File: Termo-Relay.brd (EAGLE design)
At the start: 53 x 61.6 mm, 50 parts, among them CN1 PBS-2-VERTICAL, CN2 PBS-2-VERTICAL, CN3 PBS-2-VERTICAL, CN5 PBS-4-VERTICAL, IC1 74HCT595D, IC2 74HCT595D, IC3 STM8S103FP, Q2 16M, T1 2N2222, T2 2N2222, T3 2N2222, T4 2N2222

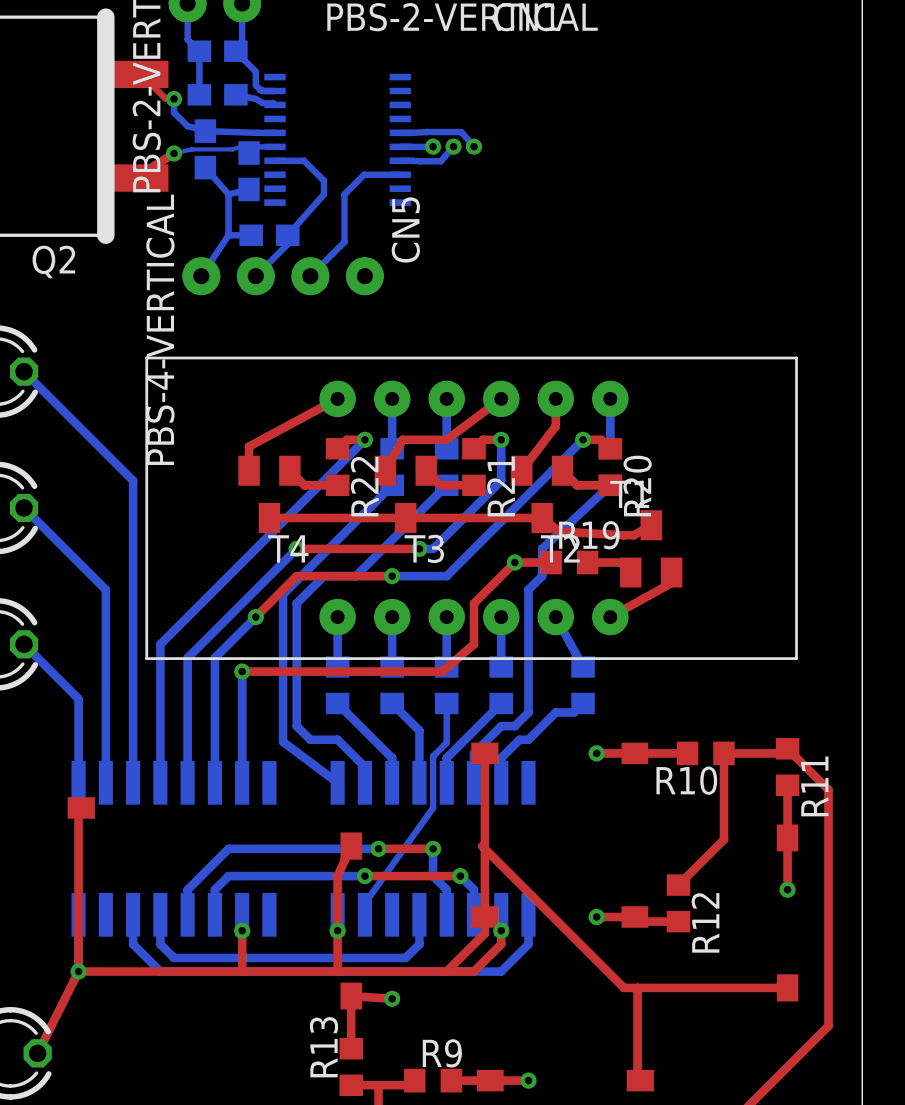
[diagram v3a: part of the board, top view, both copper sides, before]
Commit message: Roads for RCK, SCK and SER (between stm8 and hc595) were added
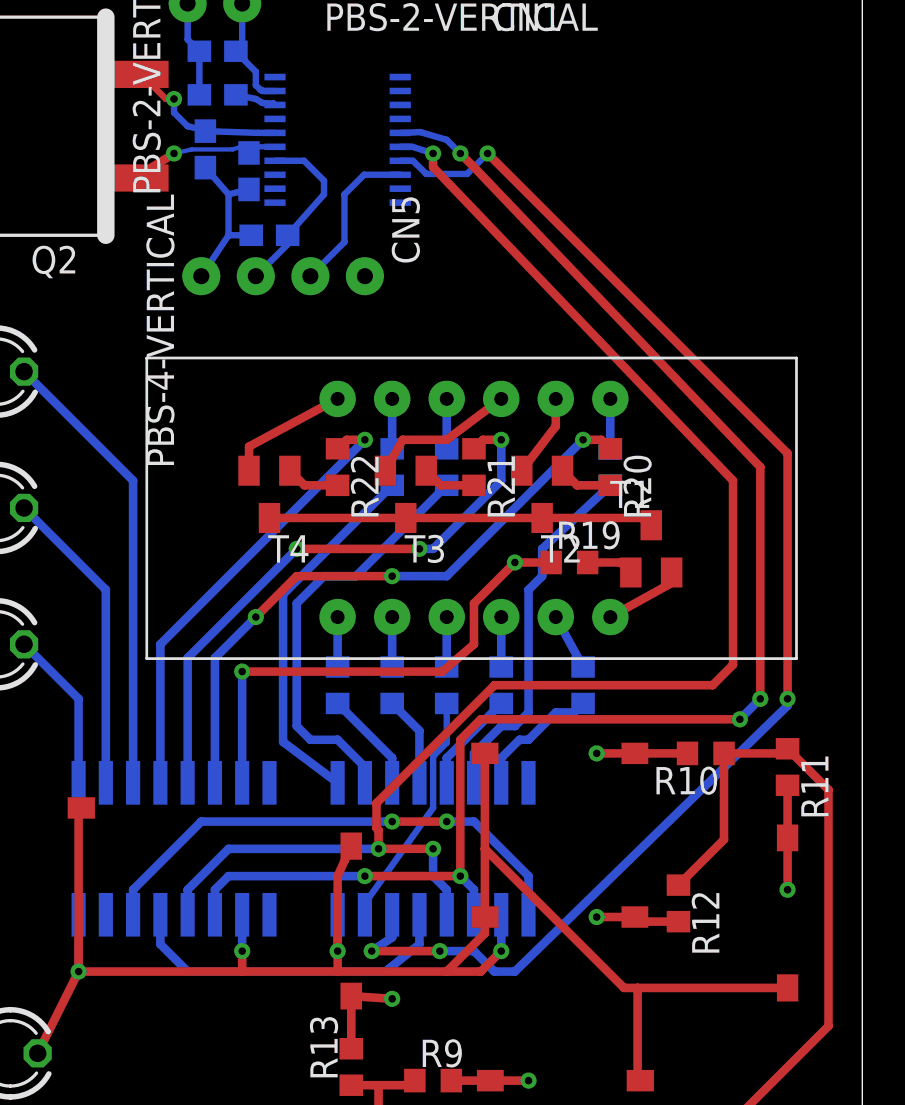
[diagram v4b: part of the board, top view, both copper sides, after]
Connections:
- net RCK: now also IC3.16; no longer IC3.15
- net SCK: now also IC3.15; no longer IC3.16
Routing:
- net SER: track 3.53 -> 63.2 mm, vias 1 -> 4
- net SCK: track 16.5 -> 70.2 mm, vias 3 -> 5
- net RCK: track 20.5 -> 69.2 mm
- net N$1: track 22.2 -> 23.8 mm, vias 0 -> 2
- net VCC: track 101.3 -> 102.1 mm

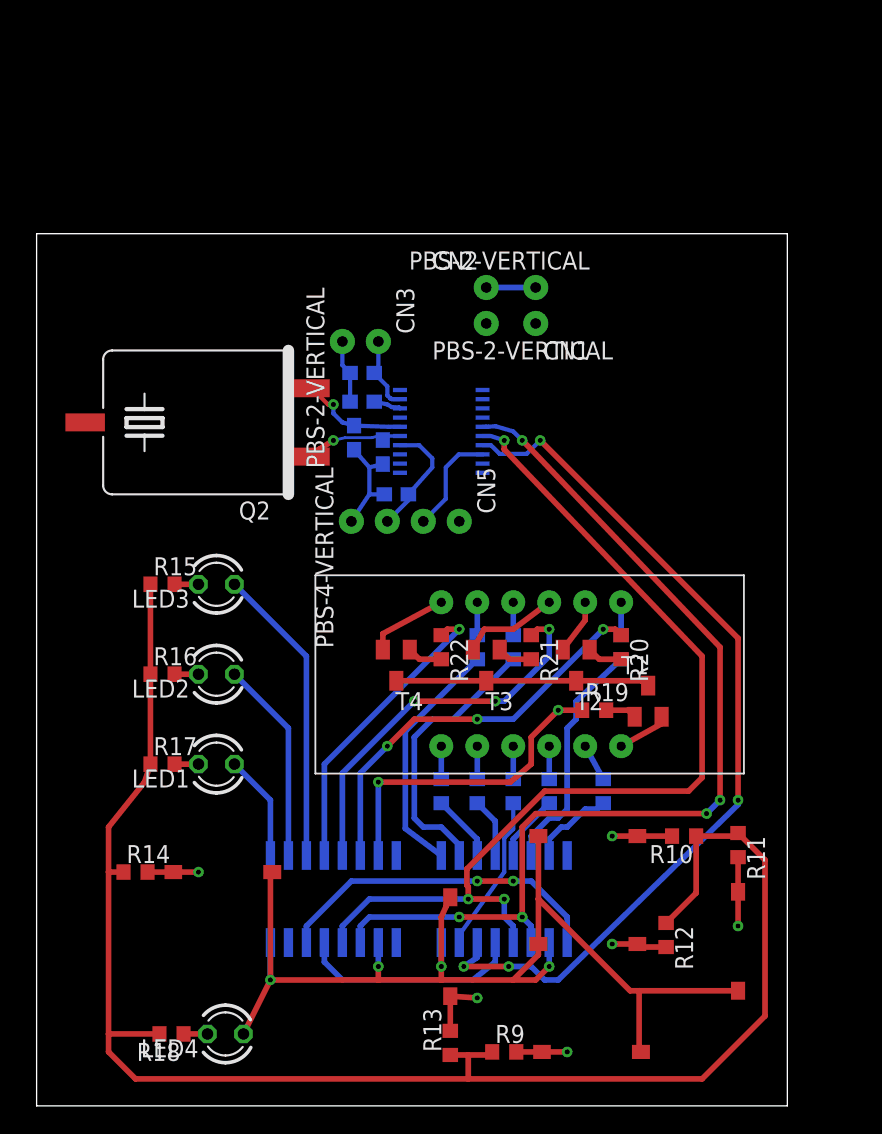
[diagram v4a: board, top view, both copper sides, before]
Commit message: size of the board was smalled
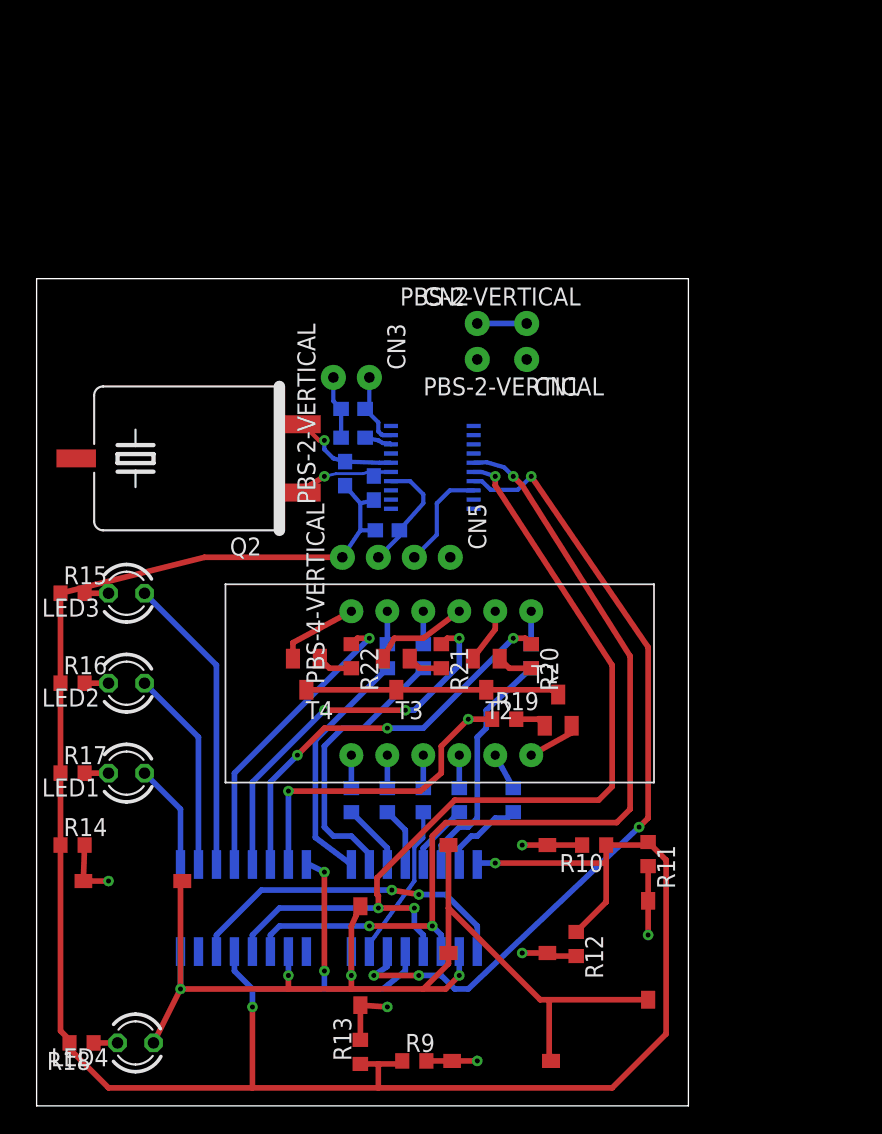
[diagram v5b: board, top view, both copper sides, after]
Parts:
- moved BTN4 6.38 mm to (22.9, 7.62)
- moved BTN5 6.38 mm to (43.2, 14.0)
- moved BTN6 6.38 mm to (29.8, 3.17)
- moved DISPLAY1 6.38 mm to (29.8, 29.8)
- moved IC1 6.38 mm to (26.7, 14.0)
- moved R1 6.38 mm to (27.3, 21.6)
- moved R10 6.38 mm to (39.4, 18.4)
- moved R11 6.38 mm to (43.2, 17.8)
- moved R12 6.38 mm to (38.1, 11.4)
- moved R13 6.38 mm to (22.9, 3.81)
- moved R2 6.38 mm to (33.7, 21.6)
- moved R20 6.38 mm to (34.9, 31.8)
- moved R3 6.38 mm to (34.9, 31.8)
- moved R4 6.38 mm to (29.8, 21.6)
- moved R7 6.38 mm to (27.3, 31.8)
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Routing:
- net GND: track 147.8 -> 184.2 mm, vias 0 -> 4
- net RCK: track 69.2 -> 64.1 mm
- net SCK: track 70.2 -> 65.1 mm, vias 5 -> 3
- net SER: track 63.2 -> 58.2 mm
- net BTN_INDIC: track 3.59 -> 4.32 mm
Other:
- board size 53 x 61.6 mm -> 46 x 58.4 mm

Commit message: Roads for buttons and power were added. One error (center button was not connected to STM) was corrected
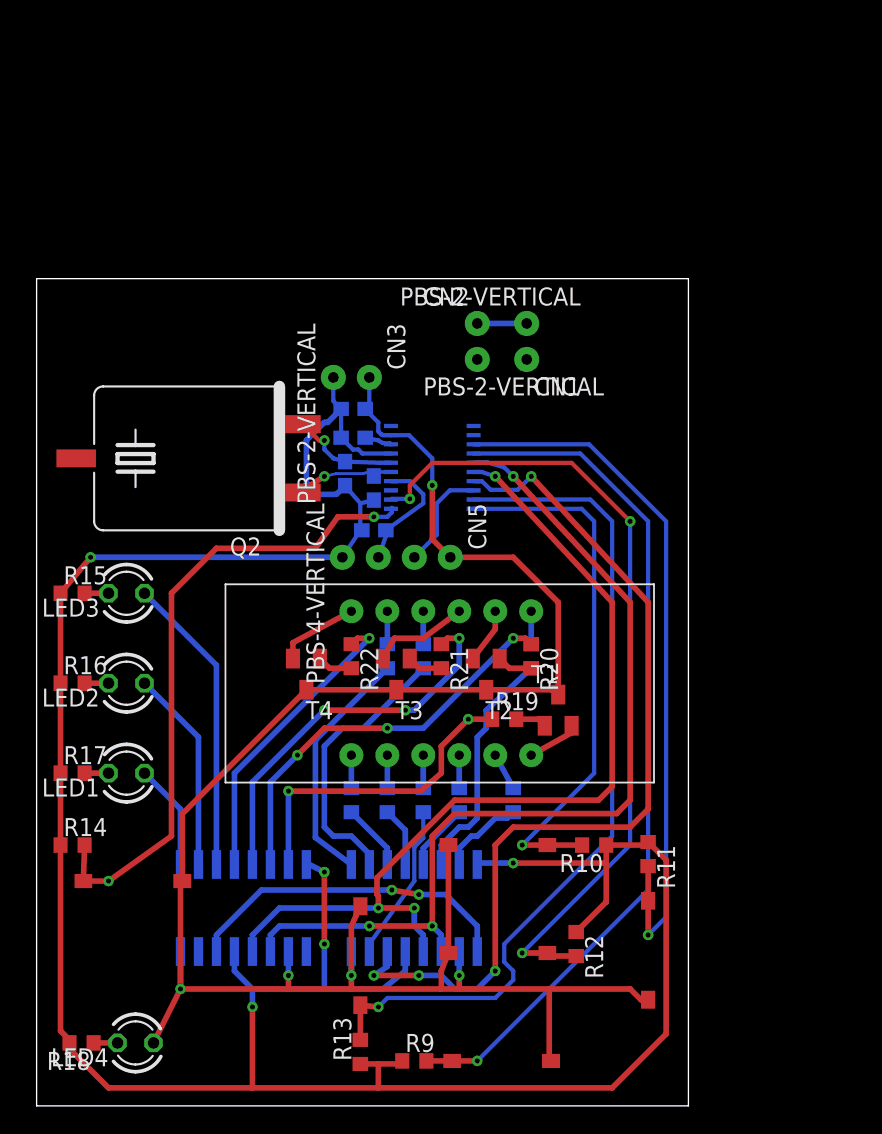
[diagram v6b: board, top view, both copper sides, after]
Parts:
- moved C1 0.95 mm to (23.8, 40.6)
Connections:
- net BTN_BOTTOM: now also IC3.14; no longer IC3.20
- net BTN_CENTER: now also IC3.2
- net BTN_LEFT: now also IC3.19; no longer IC3.14
- net BTN_TOP: now also IC3.20; no longer IC3.19
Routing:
- net BTN_BOTTOM: track 3.59 -> 61.0 mm
- net BTN_LEFT: track 4.36 -> 60.3 mm
- net BTN_CENTER: track 3.86 -> 57.7 mm, vias 1 -> 3
- net BTN_RIGHT: track 4.87 -> 50.4 mm
- net VCC: track 102.1 -> 143.4 mm, vias 4 -> 5
- net BTN_INDIC: track 4.32 -> 45.5 mm, vias 1 -> 2
- net BTN_TOP: track 4.23 -> 38.1 mm
- net GND: track 184.2 -> 197.9 mm, vias 4 -> 5
- net SER: track 58.2 -> 63.9 mm
- net RCK: track 64.1 -> 64.9 mm

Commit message: Tracing was finished.
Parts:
- moved CN2 6.84 mm to (33.7, 48.9), turned to 270 degrees
- moved CN3 5.68 mm to (28.6, 48.9)
- moved CN1 5.62 mm to (38.7, 48.9), turned to 270 degrees
- moved C2 0.64 mm to (22.4, 46.5)
- moved C4 0.64 mm to (21.8, 44.0)
- moved LED1 0.64 mm to (6.35, 22.9)
- moved R1 0.64 mm to (27.3, 21.0)
- moved R11 0.64 mm to (43.2, 17.1)
- moved R17 0.64 mm to (2.54, 22.9)
- moved R2 0.64 mm to (33.7, 21.0)
- moved R20 0.64 mm to (34.9, 31.1)
- moved R21 0.64 mm to (28.6, 31.1)
- moved R22 0.64 mm to (22.2, 31.1)
- moved R3 0.64 mm to (34.9, 31.1)
- moved R4 0.64 mm to (29.8, 21.0)
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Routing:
- net N$18: track 0.00 -> 17.3 mm, vias 0 -> 1
- net GND: track 197.9 -> 208.0 mm
- net N$20: track 0.00 -> 7.13 mm, vias 0 -> 2
- net VCC: track 143.4 -> 146.4 mm
- net BTN_CENTER: track 57.7 -> 59.9 mm
- net N$19: track 8.56 -> 9.66 mm
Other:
- board size 46 x 58.4 mm -> 46 x 52.1 mm
